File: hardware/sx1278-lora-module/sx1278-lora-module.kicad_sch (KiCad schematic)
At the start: 1 part, among them J1 Conn_01x16

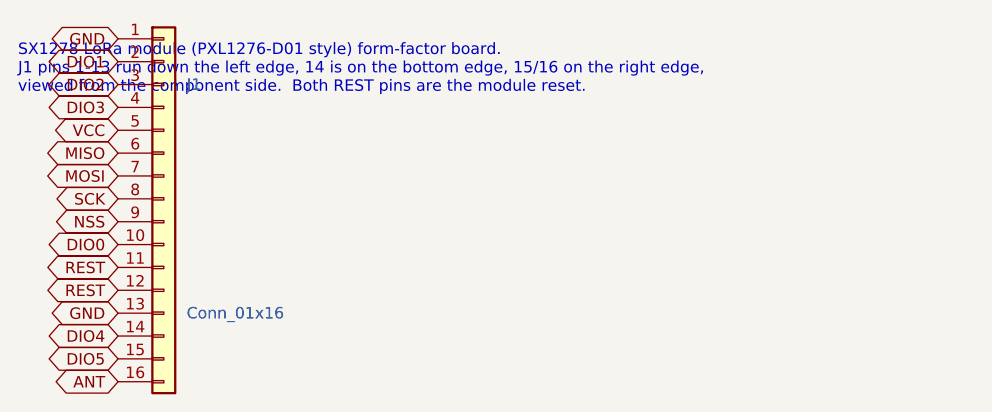
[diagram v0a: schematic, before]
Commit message: SX1278 module: correct pad layout and pin names from the pinout photo
The seller's dimensioned pinout photo shows 12 keyhole pads along one
edge, two small castellation-only notches (DIO4, DIO5) on the adjacent
edge at the shared corner, and two keyhole pads (ANT, GND) at the
opposite corner.  Pin names in physical order are GND DIO1 DIO2 DIO3
VCC MISO MOSI SCK NSS DIO0 REST GND, DIO4 DIO5, GND ANT; the seller's
table duplicated REST and shifted its tail.  Positions re-measured
from the top-down photo: row holes 1.2 mm in from the edge starting
1.2 mm from the corner, notches at 1.25/2.7 mm, ANT/GND at 1.4/2.8 mm.

Co-Authored-By: Claude Fable 5.1 <noreply@anthropic.com>
Claude-Session: https://claude.ai/code/session_01JoGdh4Cg3VtTTDZi4gQuiN
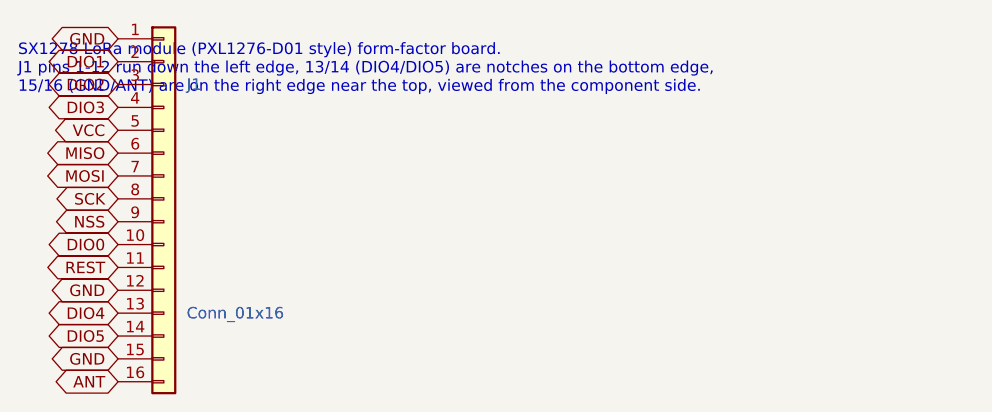
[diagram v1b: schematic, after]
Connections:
- net DIO4: now also J1.13 (Pin_13); no longer J1.14 (Pin_14)
- net DIO5: now also J1.14 (Pin_14); no longer J1.15 (Pin_15)
- net GND: now also J1.12 (Pin_12), J1.15 (Pin_15); no longer J1.13 (Pin_13)
- net REST: no longer J1.12 (Pin_12)
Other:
- note added: "SX1278 LoRa module (PXL1276-D01 style) form-factor board. J1 pins 1-12 run down the left edge, 13/14 (DIO4/DIO5) are notches on the bottom edge, 15/16 (GND/ANT) are on the right edge near the top, viewed from the component side."
- note removed: "SX1278 LoRa module (PXL1276-D01 style) form-factor board. J1 pins 1-13 run down the left edge, 14 is on the bottom edge, 15/16 on the right edge, viewed from the component side. Both REST pins are the module reset."
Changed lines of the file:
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@@
 		)
 	)
-	(global_label "REST"
+	(global_label "GND"
 		(shape bidirectional)
 		(at 71.12 111.76 180)
@@
 		)
 	)
-	(global_label "GND"
+	(global_label "DIO4"
 		(shape bidirectional)
 		(at 71.12 114.3 180)
@@
 		)
 	)
-	(global_label "DIO4"
+	(global_label "DIO5"
 		(shape bidirectional)
 		(at 71.12 116.84 180)
@@
 		)
 	)
-	(global_label "DIO5"
+	(global_label "GND"
 		(shape bidirectional)
 		(at 71.12 119.38 180)
@@
 		)
 	)
-	(text "SX1278 LoRa module (PXL1276-D01 style) form-factor board.\nJ1 pins 1-13 run down the left edge, 14 is on the bottom edge, 15/16 on the right edge,\nviewed from the component side.  Both REST pins are the module reset."
+	(text "SX1278 LoRa module (PXL1276-D01 style) form-factor board.\nJ1 pins 1-12 run down the left edge, 13/14 (DIO4/DIO5) are notches on the bottom edge,\n15/16 (GND/ANT) are on the right edge near the top, viewed from the component side."
 		(exclude_from_sim no)
 		(at 60 90 0)
